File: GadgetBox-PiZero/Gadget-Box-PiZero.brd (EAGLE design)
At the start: 93.5 x 53.5 mm, 9 parts

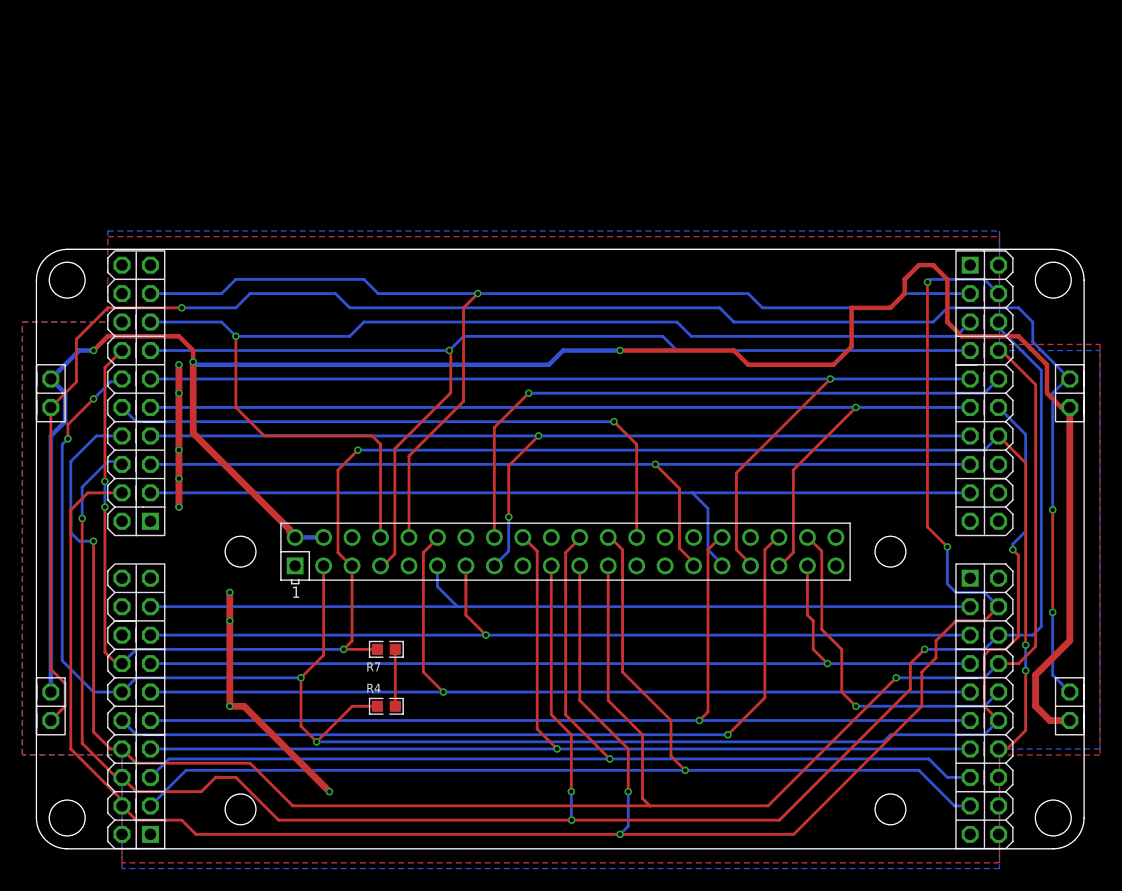
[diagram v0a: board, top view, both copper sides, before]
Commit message: Fixed Silkscreen - Pizero
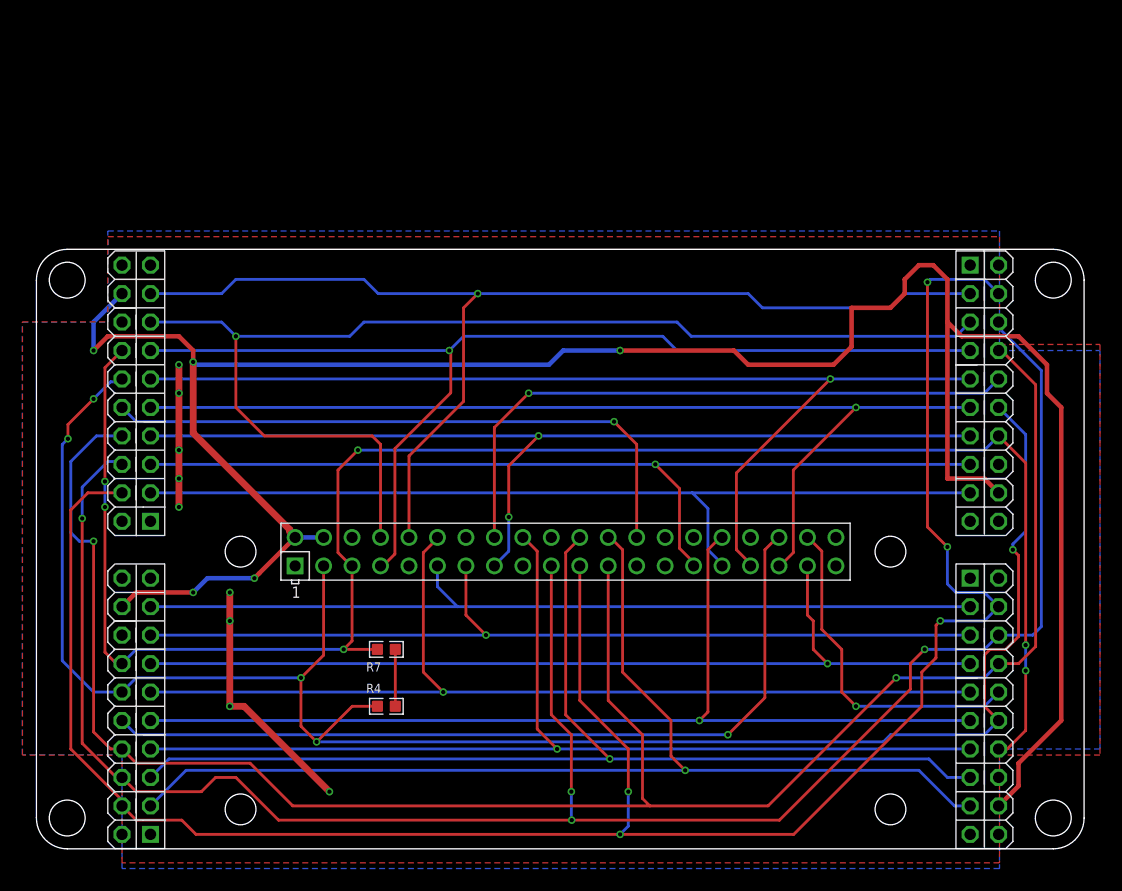
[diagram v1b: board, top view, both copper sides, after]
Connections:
- removed net RESET: AH.RESET@2, AL.RESET@2, BH.RESET@2, BL.RESET@2
- net 5V0: now also AH.5V@B7, AL.5V@B7, BH.5V@B7, BL.5V@B7; no longer AH.5V@2, AL.5V@2, BH.5V@2, BL.5V@2
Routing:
- net RESET: track 161.0 -> 0.00 mm, vias 3 -> 0
- net 5V0: track 193.1 -> 208.1 mm, vias 3 -> 5
- net SPI-MISO: track 190.0 -> 190.8 mm, vias 4 -> 5

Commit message: Added charging circuit.
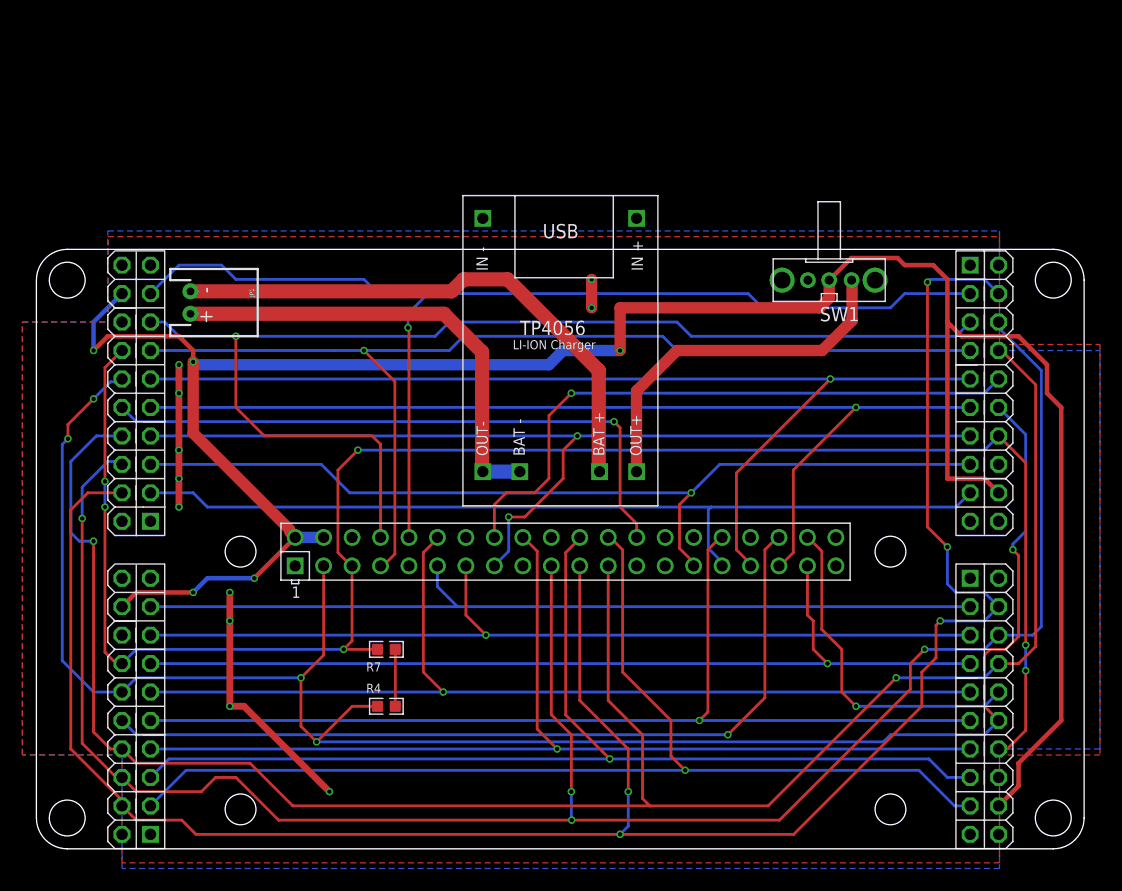
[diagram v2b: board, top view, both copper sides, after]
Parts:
- added JP1: (no value), SparkFun:JST-2-PTH-NS
- added SW1: OS102011MA1Q, adafruit:OS102011MA1Q
- added U$2: TP4056, TP4056 charging module:TP4056
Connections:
- new net N$2: JP1.1, U$2.BAT+
- new net N$3: SW1.1, U$2.OUT+
- net 5V0: now also SW1.2
- net GND: now also JP1.2, U$2.BAT-, U$2.OUT-
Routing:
- net N$2: track 0.00 -> 49.3 mm
- net GND: track 34.9 -> 78.9 mm, vias 9 -> 11
- net N$3: track 0.00 -> 32.7 mm
- net D5: track 86.4 -> 88.7 mm
- net D2: track 96.2 -> 95.2 mm
- net D6: track 83.6 -> 82.7 mm
- net SPI-CSB: track 56.6 -> 55.9 mm
- net D0/RX/MISO: track 99.6 -> 98.8 mm
- net D7: track 80.8 -> 80.1 mm
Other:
- board text added: "Gadget Box - Pi Zero Copyright 2016 Gadget Factory, LLC Version 1.0-M"
- board text removed: "Gadget Box - Pi Zero Copyright 2016 Gadget Factory, LLC Version 1.1"

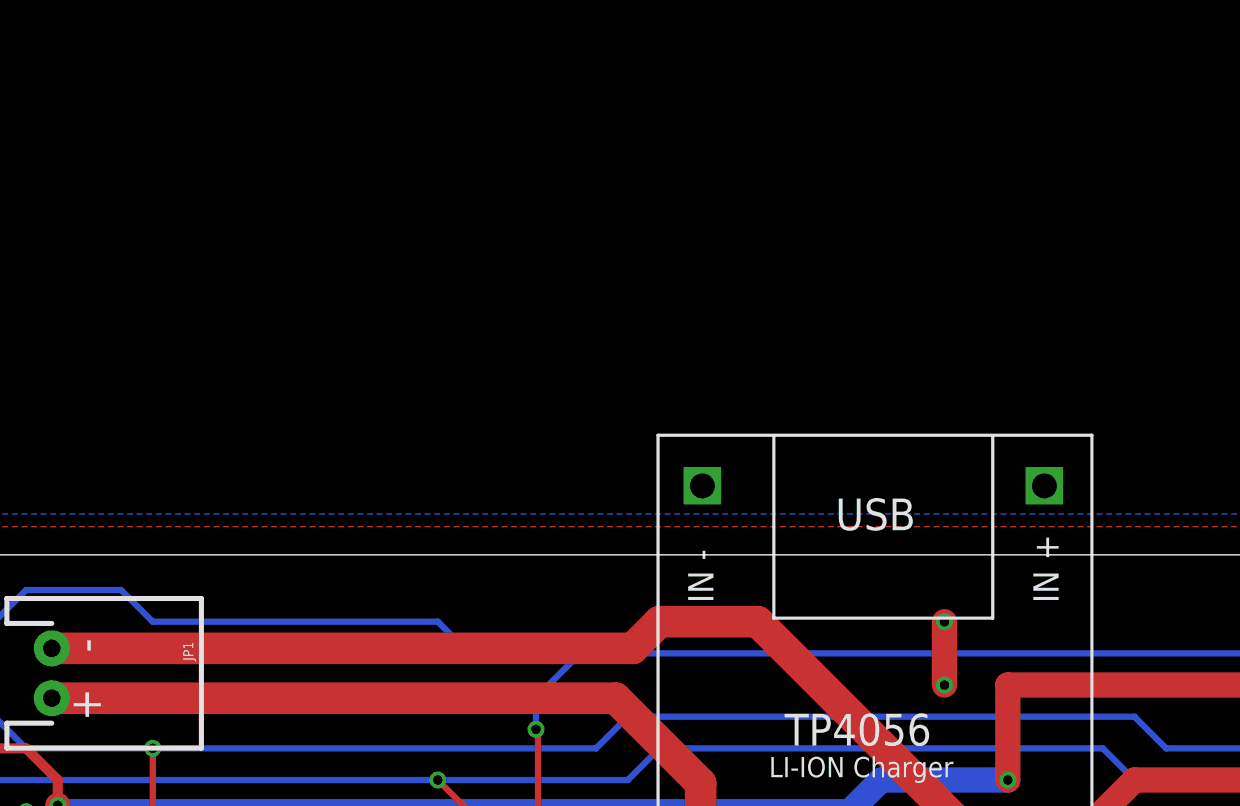
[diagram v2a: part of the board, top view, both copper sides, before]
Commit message: Add battery wire cutout.
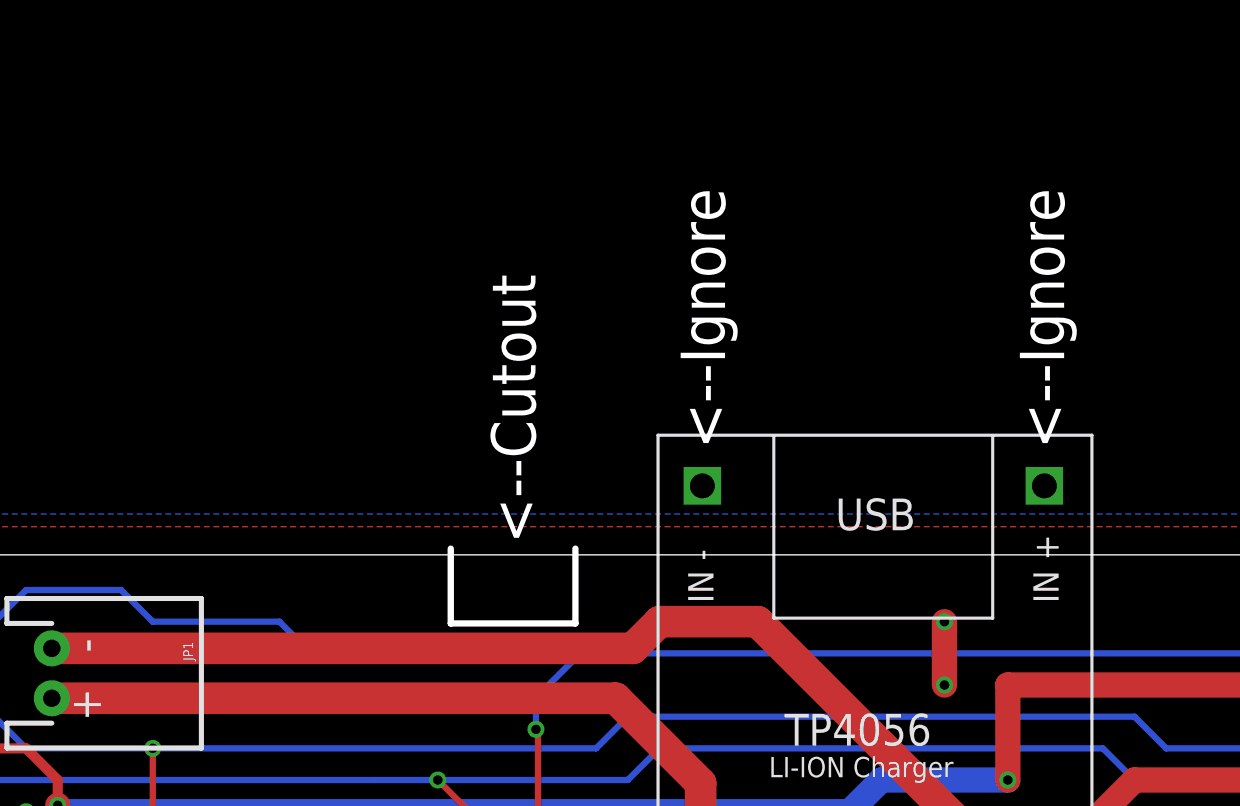
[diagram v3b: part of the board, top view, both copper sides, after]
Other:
- board text added: "<--Cutout"
- board text added: "<--Ignore"
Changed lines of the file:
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@@
 <grid distance="0.05" unitdist="inch" unit="inch" style="lines" multiple="1" display="yes" altdistance="0.005" altunitdist="inch" altunit="inch"/>
 <layers>
-<layer number="1" name="Top" color="4" fill="1" visible="no" active="yes"/>
+<layer number="1" name="Top" color="4" fill="1" visible="yes" active="yes"/>
 <layer number="2" name="Route2" color="1" fill="3" visible="no" active="no"/>
 <layer number="3" name="Route3" color="4" fill="3" visible="no" active="no"/>
 <layer number="14" name="Route14" color="1" fill="6" visible="no" active="no"/>
 <layer number="15" name="Route15" color="4" fill="6" visible="no" active="no"/>
-<layer number="16" name="Bottom" color="1" fill="1" visible="no" active="yes"/>
+<layer number="16" name="Bottom" color="1" fill="1" visible="yes" active="yes"/>
 <layer number="17" name="Pads" color="2" fill="1" visible="yes" active="yes"/>
 <layer number="18" name="Vias" color="2" fill="1" visible="yes" active="yes"/>
@@
 <layer number="20" name="Dimension" color="15" fill="1" visible="yes" active="yes"/>
 <layer number="21" name="tPlace" color="16" fill="1" visible="yes" active="yes"/>
-<layer number="22" name="bPlace" color="14" fill="1" visible="no" active="yes"/>
-<layer number="23" name="tOrigins" color="15" fill="1" visible="no" active="yes"/>
+<layer number="22" name="bPlace" color="14" fill="1" visible="yes" active="yes"/>
+<layer number="23" name="tOrigins" color="15" fill="1" visible="yes" active="yes"/>
 <layer number="24" name="bOrigins" color="15" fill="1" visible="yes" active="yes"/>
-<layer number="25" name="tNames" color="16" fill="1" visible="no" active="yes"/>
-<layer number="26" name="bNames" color="7" fill="1" visible="yes" active="yes"/>
+<layer number="25" name="tNames" color="16" fill="1" visible="yes" active="yes"/>
+<layer number="26" name="bNames" color="7" fill="1" visible="no" active="yes"/>
 <layer number="27" name="tValues" color="7" fill="1" visible="no" active="yes"/>
 <layer number="28" name="bValues" color="7" fill="1" visible="no" active="yes"/>
@@
 <layer number="30" name="bStop" color="7" fill="6" visible="no" active="yes"/>
 <layer number="31" name="tCream" color="7" fill="4" visible="no" active="yes"/>
-<layer number="32" name="bCream" color="7" fill="5" visible="yes" active="yes"/>
+<layer number="32" name="bCream" color="7" fill="5" visible="no" active="yes"/>
 <layer number="33" name="tFinish" color="6" fill="3" visible="no" active="yes"/>
 <layer number="34" name="bFinish" color="6" fill="6" visible="no" active="yes"/>
@@
 <layer number="49" name="Reference" color="7" fill="1" visible="no" active="yes"/>
 <layer number="50" name="dxf" color="7" fill="1" visible="no" active="yes"/>
-<layer number="51" name="tDocu" color="6" fill="1" visible="no" active="yes"/>
-<layer number="52" name="bDocu" color="7" fill="1" visible="yes" active="yes"/>
+<layer number="51" name="tDocu" color="6" fill="1" visible="yes" active="yes"/>
+<layer number="52" name="bDocu" color="7" fill="1" visible="no" active="yes"/>
 <layer number="53" name="tGND_GNDA" color="7" fill="1" visible="no" active="yes"/>
 <layer number="54" name="bGND_GNDA" color="7" fill="1" visible="no" active="yes"/>
@@
 <layer number="196" name="mValues" color="7" fill="1" visible="no" active="yes"/>
 <layer number="199" name="Contour" color="7" fill="1" visible="no" active="yes"/>
-<layer number="200" name="200bmp" color="1" fill="1" visible="yes" active="yes"/>
+<layer number="200" name="200bmp" color="1" fill="1" visible="no" active="yes"/>
 <layer number="201" name="201bmp" color="7" fill="1" visible="no" active="yes"/>
 <layer number="202" name="202bmp" color="7" fill="1" visible="no" active="yes"/>
@@
 <wire x1="49.007" y1="26.416" x2="89.9006" y2="26.416" width="0.254" layer="200"/>
 <wire x1="49.007" y1="26.67" x2="89.1722" y2="26.67" width="0.254" layer="200"/>
+<wire x1="36" y1="55" x2="36" y2="52" width="0.254" layer="20"/>
+<wire x1="36" y1="52" x2="31" y2="52" width="0.254" layer="20"/>
+<wire x1="31" y1="52" x2="31" y2="55" width="0.254" layer="20"/>
+<text x="34.4" y="55.2" size="1.778" layer="20" font="vector" ratio="15" rot="R90">&lt;--Cutout</text>
+<text x="42" y="59" size="1.778" layer="20" font="vector" ratio="15" rot="R90">&lt;--Ignore</text>
+<text x="55.6" y="59" size="1.778" layer="20" font="vector" ratio="15" rot="R90">&lt;--Ignore</text>
 </plain>
 <attributes>
@@
 <wire x1="66.04" y1="49.53" x2="64.77" y2="50.8" width="0.254" layer="16"/>
 <wire x1="64.77" y1="50.8" x2="36.195" y2="50.8" width="0.254" layer="16"/>
-<wire x1="36.195" y1="50.8" x2="31.75" y2="50.8" width="0.254" layer="16"/>
-<wire x1="31.75" y1="50.8" x2="30.48" y2="52.07" width="0.254" layer="16"/>
-<wire x1="30.48" y1="52.07" x2="19.05" y2="52.07" width="0.254" layer="16"/>
 <contactref element="U$1" pad="10"/>
 <wire x1="34.5" y1="29.04" x2="34.5" y2="47.669" width="0.254" layer="1"/>
@@
 <wire x1="13.97" y1="53.34" x2="17.78" y2="53.34" width="0.254" layer="16"/>
 <wire x1="17.78" y1="53.34" x2="19.05" y2="52.07" width="0.254" layer="16"/>
+<wire x1="19.05" y1="52.07" x2="24.13" y2="52.07" width="0.254" layer="16"/>
+<wire x1="24.13" y1="52.07" x2="25.4" y2="50.8" width="0.254" layer="16"/>
+<wire x1="25.4" y1="50.8" x2="36.195" y2="50.8" width="0.254" layer="16"/>
 </signal>
 <signal name="D4*">
